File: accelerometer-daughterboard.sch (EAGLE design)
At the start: 21 parts, among them Q2 BSS138, U1 LIS3DHTR, U2 AP2112K-3.3

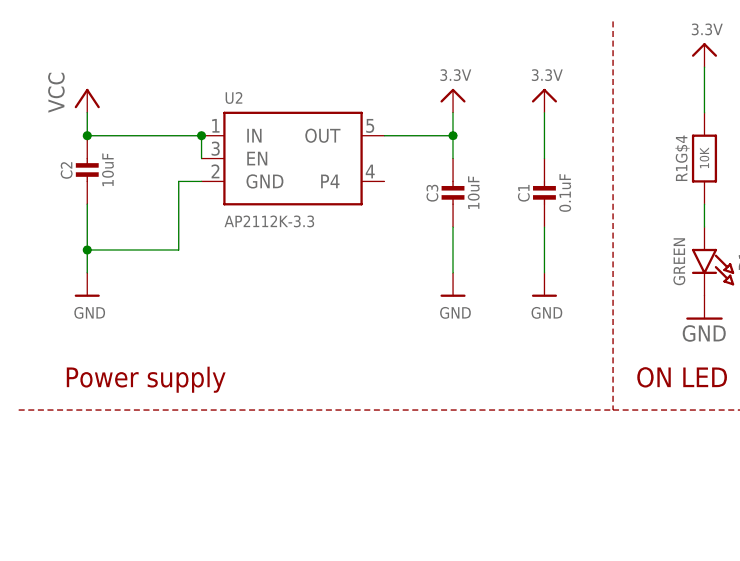
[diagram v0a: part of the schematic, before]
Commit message: Remove power supply (have 3.3 V already)
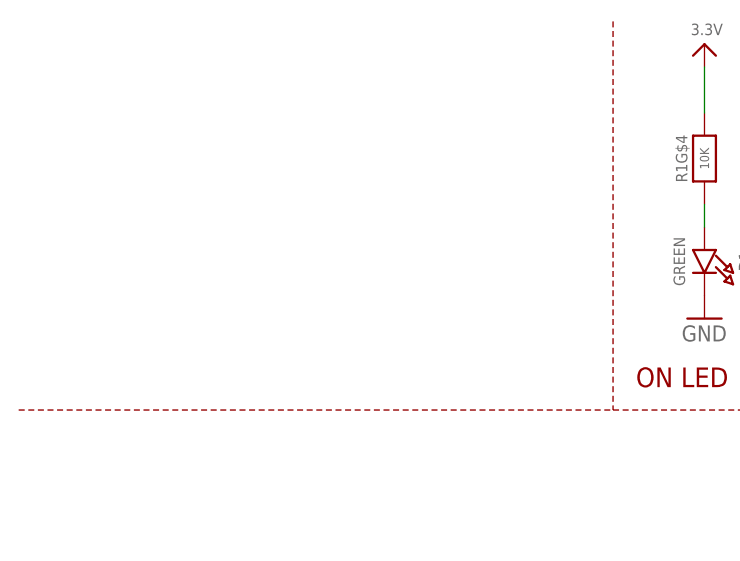
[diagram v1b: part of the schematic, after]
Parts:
- removed C1: 0.1uF, microbuilder:CAP_CERAMIC0603_NO
- removed C2, C3: 10uF, microbuilder:CAP_CERAMIC0805-NOOUTLINE
- removed U2: AP2112K-3.3, microbuilder:VREG_SOT23-5
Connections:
- net 3.3V: no longer C1.1, C3.1, U2.OUT
- net GND: no longer C1.2, C2.2, C3.2, U2.GND
- net VCC: no longer C2.1, U2.EN, U2.IN
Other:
- note removed: "Power supply"
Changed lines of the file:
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@@
 <?xml version="1.0" encoding="utf-8"?>
 <!DOCTYPE eagle SYSTEM "eagle.dtd">
-<eagle version="9.6.1">
+<eagle version="9.6.2">
 <drawing>
 <settings>
@@
 </classes>
 <parts>
-<part name="U$13" library="microbuilder" deviceset="GND" device=""/>
-<part name="C2" library="microbuilder" deviceset="CAP_CERAMIC" device="0805-NOOUTLINE" value="10uF"/>
-<part name="U2" library="microbuilder" deviceset="VREG_SOT23-5" device="" value="AP2112K-3.3"/>
-<part name="C3" library="microbuilder" deviceset="CAP_CERAMIC" device="0805-NOOUTLINE" value="10uF"/>
-<part name="U$5" library="microbuilder" deviceset="GND" device=""/>
-<part name="U$6" library="microbuilder" deviceset="GND" device=""/>
-<part name="C1" library="microbuilder" deviceset="CAP_CERAMIC" device="0603_NO" value="0.1uF"/>
-<part name="U$14" library="microbuilder" deviceset="3.3V" device=""/>
-<part name="U$15" library="microbuilder" deviceset="3.3V" device=""/>
 <part name="U$7" library="microbuilder" deviceset="3.3V" device=""/>
 <part name="U$24" library="microbuilder" deviceset="3.3V" device=""/>
@@
 <part name="P+1" library="supply1" library_urn="urn:adsk.eagle:library:371" deviceset="VCC" device=""/>
 <part name="P+2" library="supply1" library_urn="urn:adsk.eagle:library:371" deviceset="VCC" device=""/>
-<part name="P+3" library="supply1" library_urn="urn:adsk.eagle:library:371" deviceset="VCC" device=""/>
 <part name="U$3" library="microbuilder" deviceset="3.3V" device=""/>
 <part name="U1" library="microbuilder" deviceset="ACCEL_LIS3DHTR" device="" value="LIS3DHTR"/>
@@
 <text x="132.08" y="139.7" size="1.778" layer="91">D</text>
 <text x="71.12" y="134.62" size="2.1844" layer="94" ratio="7">ON LED</text>
-<text x="7.62" y="134.62" size="2.1844" layer="94" ratio="7">Power supply</text>
 <text x="177.8" y="76.2" size="1.778" layer="97">I2C</text>
 <text x="162.56" y="71.12" size="1.778" layer="97">SCL (Pin 4) = Serial Clock</text>
@@
 <attribute name="VALUE" x="76.2" y="139.7" size="1.778" layer="96"/>
 </instance>
-<instance part="U$13" gate="G$1" x="10.16" y="144.78" smashed="yes">
-<attribute name="VALUE" x="8.636" y="142.24" size="1.27" layer="96"/>
-</instance>
-<instance part="C2" gate="G$1" x="10.16" y="157.48" smashed="yes">
-<attribute name="NAME" x="7.87" y="158.73" size="1.27" layer="95" font="vector" rot="R90" align="center"/>
-<attribute name="VALUE" x="12.46" y="158.73" size="1.27" layer="96" font="vector" rot="R90" align="center"/>
-</instance>
-<instance part="U2" gate="G$1" x="33.02" y="160.02" smashed="yes">
-<attribute name="NAME" x="25.4" y="166.116" size="1.27" layer="95"/>
-<attribute name="VALUE" x="25.4" y="152.4" size="1.27" layer="95"/>
-</instance>
-<instance part="C3" gate="G$1" x="50.8" y="154.94" smashed="yes">
-<attribute name="NAME" x="48.51" y="156.19" size="1.27" layer="95" font="vector" rot="R90" align="center"/>
-<attribute name="VALUE" x="53.1" y="156.19" size="1.27" layer="96" font="vector" rot="R90" align="center"/>
-</instance>
-<instance part="U$5" gate="G$1" x="50.8" y="144.78" smashed="yes">
-<attribute name="VALUE" x="49.276" y="142.24" size="1.27" layer="96"/>
-</instance>
-<instance part="U$6" gate="G$1" x="60.96" y="144.78" smashed="yes">
-<attribute name="VALUE" x="59.436" y="142.24" size="1.27" layer="96"/>
-</instance>
-<instance part="C1" gate="G$1" x="60.96" y="154.94" smashed="yes">
-<attribute name="NAME" x="58.67" y="156.19" size="1.27" layer="95" font="vector" rot="R90" align="center"/>
-<attribute name="VALUE" x="63.26" y="156.19" size="1.27" layer="96" font="vector" rot="R90" align="center"/>
-</instance>
-<instance part="U$14" gate="G$1" x="60.96" y="167.64" smashed="yes">
-<attribute name="VALUE" x="59.436" y="168.656" size="1.27" layer="96"/>
-</instance>
-<instance part="U$15" gate="G$1" x="50.8" y="167.64" smashed="yes">
-<attribute name="VALUE" x="49.276" y="168.656" size="1.27" layer="96"/>
-</instance>
 <instance part="U$7" gate="G$1" x="165.1" y="170.18" smashed="yes" rot="MR0">
 <attribute name="VALUE" x="166.624" y="171.196" size="1.27" layer="96" rot="MR0"/>
@@
 <instance part="P+2" gate="VCC" x="129.54" y="170.18" smashed="yes">
 <attribute name="VALUE" x="127" y="167.64" size="1.778" layer="96" rot="R90"/>
-</instance>
-<instance part="P+3" gate="VCC" x="10.16" y="167.64" smashed="yes">
-<attribute name="VALUE" x="7.62" y="165.1" size="1.778" layer="96" rot="R90"/>
 </instance>
 <instance part="U$3" gate="G$1" x="78.74" y="172.72" smashed="yes">
@@
 <wire x1="238.76" y1="157.48" x2="205.74" y2="157.48" width="0.1524" layer="91"/>
 <label x="220.98" y="157.48" size="1.778" layer="95"/>
-</segment>
-<segment>
-<wire x1="22.86" y1="157.48" x2="20.32" y2="157.48" width="0.1524" layer="91"/>
-<wire x1="20.32" y1="157.48" x2="20.32" y2="149.86" width="0.1524" layer="91"/>
-<wire x1="20.32" y1="149.86" x2="10.16" y2="149.86" width="0.1524" layer="91"/>
-<wire x1="10.16" y1="149.86" x2="10.16" y2="154.94" width="0.1524" layer="91"/>
-<wire x1="10.16" y1="149.86" x2="10.16" y2="147.32" width="0.1524" layer="91"/>
-<junction x="10.16" y="149.86"/>
-<pinref part="U$13" gate="G$1" pin="GND"/>
-<pinref part="C2" gate="G$1" pin="2"/>
-<pinref part="U2" gate="G$1" pin="GND"/>
-</segment>
-<segment>
-<pinref part="C3" gate="G$1" pin="2"/>
-<pinref part="U$5" gate="G$1" pin="GND"/>
-<wire x1="50.8" y1="152.4" x2="50.8" y2="147.32" width="0.1524" layer="91"/>
-</segment>
-<segment>
-<pinref part="U$6" gate="G$1" pin="GND"/>
-<pinref part="C1" gate="G$1" pin="2"/>
-<wire x1="60.96" y1="152.4" x2="60.96" y2="147.32" width="0.1524" layer="91"/>
 </segment>
 <segment>
@@
 </segment>
 <segment>
-<wire x1="22.86" y1="162.56" x2="10.16" y2="162.56" width="0.1524" layer="91"/>
-<wire x1="10.16" y1="165.1" x2="10.16" y2="162.56" width="0.1524" layer="91"/>
-<wire x1="22.86" y1="160.02" x2="22.86" y2="162.56" width="0.1524" layer="91"/>
-<junction x="10.16" y="162.56"/>
-<junction x="22.86" y="162.56"/>
-<pinref part="C2" gate="G$1" pin="1"/>
-<pinref part="U2" gate="G$1" pin="IN"/>
-<pinref part="U2" gate="G$1" pin="EN"/>
-<pinref part="P+3" gate="VCC" pin="VCC"/>
-</segment>
-<segment>
 <wire x1="106.68" y1="121.92" x2="96.52" y2="121.92" width="0.1524" layer="91"/>
 <wire x1="96.52" y1="121.92" x2="96.52" y2="124.46" width="0.1524" layer="91"/>
@@
 <net name="3.3V" class="2">
 <segment>
-<pinref part="C1" gate="G$1" pin="1"/>
-<wire x1="60.96" y1="165.1" x2="60.96" y2="160.02" width="0.1524" layer="91"/>
-<pinref part="U$14" gate="G$1" pin="3.3V"/>
-</segment>
-<segment>
-<wire x1="43.18" y1="162.56" x2="50.8" y2="162.56" width="0.1524" layer="91"/>
-<wire x1="50.8" y1="162.56" x2="50.8" y2="165.1" width="0.1524" layer="91"/>
-<pinref part="U2" gate="G$1" pin="OUT"/>
-<pinref part="C3" gate="G$1" pin="1"/>
-<wire x1="50.8" y1="162.56" x2="50.8" y2="160.02" width="0.1524" layer="91"/>
-<junction x="50.8" y="162.56"/>
-<pinref part="U$15" gate="G$1" pin="3.3V"/>
-</segment>
-<segment>
 <pinref part="U$7" gate="G$1" pin="3.3V"/>

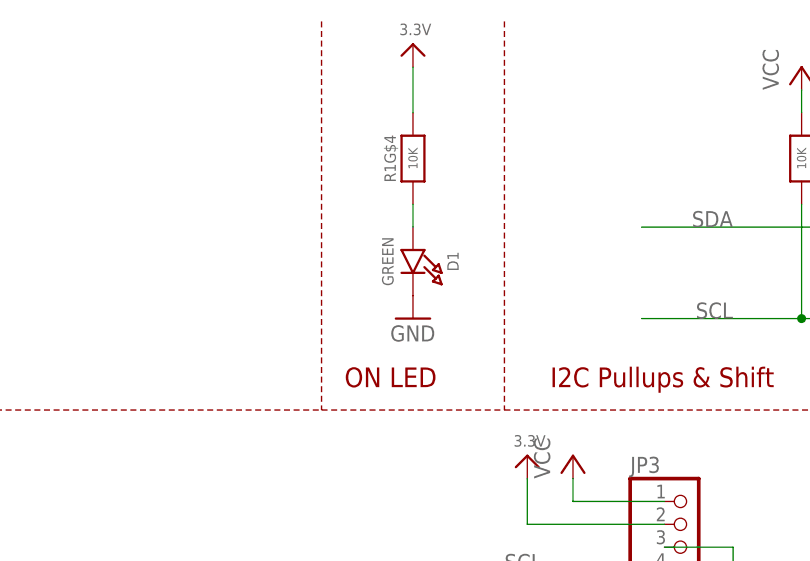
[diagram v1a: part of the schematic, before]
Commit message: Remove LED
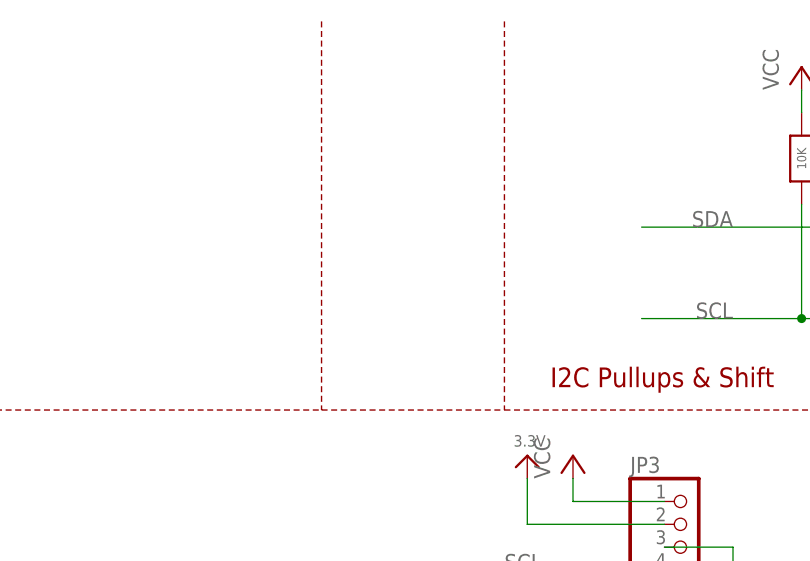
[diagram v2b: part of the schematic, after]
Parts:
- removed D1: GREEN, microbuilder:LED0603_NOOUTLINE
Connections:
- removed net N$1: D1.A, R1G$4.1
- net 3.3V: no longer R1G$4.2
- net GND: no longer D1.C
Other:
- note removed: "ON LED"
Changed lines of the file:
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@@
 <part name="U$19" library="microbuilder" deviceset="MOUNTINGHOLE" device="2.5"/>
 <part name="U$21" library="microbuilder" deviceset="MOUNTINGHOLE" device="2.5"/>
-<part name="D1" library="microbuilder" deviceset="LED" device="0603_NOOUTLINE" value="GREEN"/>
-<part name="GND6" library="supply1" library_urn="urn:adsk.eagle:library:371" deviceset="GND" device=""/>
 <part name="P+1" library="supply1" library_urn="urn:adsk.eagle:library:371" deviceset="VCC" device=""/>
 <part name="P+2" library="supply1" library_urn="urn:adsk.eagle:library:371" deviceset="VCC" device=""/>
-<part name="U$3" library="microbuilder" deviceset="3.3V" device=""/>
 <part name="U1" library="microbuilder" deviceset="ACCEL_LIS3DHTR" device="" value="LIS3DHTR"/>
 <part name="U$2" library="microbuilder" deviceset="GND" device=""/>
@@
 <text x="142.24" y="139.7" size="1.778" layer="91">S</text>
 <text x="132.08" y="139.7" size="1.778" layer="91">D</text>
-<text x="71.12" y="134.62" size="2.1844" layer="94" ratio="7">ON LED</text>
 <text x="177.8" y="76.2" size="1.778" layer="97">I2C</text>
 <text x="162.56" y="71.12" size="1.778" layer="97">SCL (Pin 4) = Serial Clock</text>
@@
 <instance part="U$19" gate="G$1" x="251.46" y="30.48" smashed="yes"/>
 <instance part="U$21" gate="G$1" x="251.46" y="22.86" smashed="yes"/>
-<instance part="D1" gate="G$1" x="78.74" y="147.32" smashed="yes" rot="R270">
-<attribute name="NAME" x="83.185" y="148.59" size="1.27" layer="95" rot="R270" align="center"/>
-<attribute name="VALUE" x="75.946" y="148.59" size="1.27" layer="96" rot="R270" align="center"/>
-</instance>
-<instance part="GND6" gate="1" x="78.74" y="142.24" smashed="yes">
-<attribute name="VALUE" x="76.2" y="139.7" size="1.778" layer="96"/>
-</instance>
 <instance part="U$7" gate="G$1" x="165.1" y="170.18" smashed="yes" rot="MR0">
 <attribute name="VALUE" x="166.624" y="171.196" size="1.27" layer="96" rot="MR0"/>
@@
 <attribute name="VALUE" x="127" y="167.64" size="1.778" layer="96" rot="R90"/>
 </instance>
-<instance part="U$3" gate="G$1" x="78.74" y="172.72" smashed="yes">
-<attribute name="VALUE" x="77.216" y="173.736" size="1.27" layer="96"/>
-</instance>
 <instance part="U1" gate="G$1" x="104.14" y="63.5" smashed="yes">
 <attribute name="NAME" x="91.44" y="78.74" size="1.27" layer="95"/>
@@
 <attribute name="NAME" x="127" y="35.56" size="1.27" layer="95" font="vector" align="center"/>
 <attribute name="VALUE" x="127" y="33.02" size="1.016" layer="96" font="vector" ratio="15" align="center"/>
-</instance>
-<instance part="R1" gate="G$4" x="78.74" y="160.02" smashed="yes" rot="R90">
-<attribute name="NAME" x="76.2" y="160.02" size="1.27" layer="95" font="vector" rot="R90" align="center"/>
-<attribute name="VALUE" x="78.74" y="160.02" size="1.016" layer="96" font="vector" ratio="15" rot="R90" align="center"/>
 </instance>
 <instance part="R1" gate="G$2" x="134.62" y="43.18" smashed="yes" rot="R90">
@@
 <wire x1="238.76" y1="157.48" x2="205.74" y2="157.48" width="0.1524" layer="91"/>
 <label x="220.98" y="157.48" size="1.778" layer="95"/>
-</segment>
-<segment>
-<pinref part="GND6" gate="1" pin="GND"/>
-<pinref part="D1" gate="G$1" pin="C"/>
 </segment>
 <segment>
@@
 </segment>
 <segment>
-<pinref part="U$3" gate="G$1" pin="3.3V"/>
-<wire x1="78.74" y1="170.18" x2="78.74" y2="165.1" width="0.1524" layer="91"/>
-<pinref part="R1" gate="G$4" pin="2"/>
-</segment>
-<segment>
 <pinref part="U1" gate="G$1" pin="VDD"/>
 <pinref part="U$8" gate="G$1" pin="3.3V"/>
@@
 </segment>
 </net>
-<net name="N$1" class="0">
-<segment>
-<pinref part="D1" gate="G$1" pin="A"/>
-<wire x1="78.74" y1="152.4" x2="78.74" y2="154.94" width="0.1524" layer="91"/>
-<pinref part="R1" gate="G$4" pin="1"/>
-</segment>
-</net>
